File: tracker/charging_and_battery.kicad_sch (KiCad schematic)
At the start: 13 parts, among them J1 USB_C_Receptacle_PowerOnly_6P, Q1 DMG9926UDM-7, U3 DW01A, U5 TP4056-42-ESOP8

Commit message: added led's
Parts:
- added D1, D2: LED, LED_SMD:LED_0603_1608Metric, symbol Device:LED
- added R10, R8: 680, Resistor_SMD:R_0603_1608Metric, symbol Device:R
- J1: footprint Package_DFN_QFN:QFN-24-1EP_4x4mm_P0.5mm_EP2.7x2.7mm -> Connector_USB:USB_C_Receptacle_HRO_TYPE-C-31-M-12
- R4: value 2.4k -> 1.2k
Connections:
- net at C5.1, J1.A9 (VBUS), J1.B9 (VBUS)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: now also R10.1, R8.1
- net at U5.6 (~{STDBY}): now also D2.1 (K)
- net at U5.7 (~{CHRG}): now also D1.1 (K)
- new net: D2.2 (A), R10.2
- new net: D1.2 (A), R8.2
- no-connect marks 2 -> 0

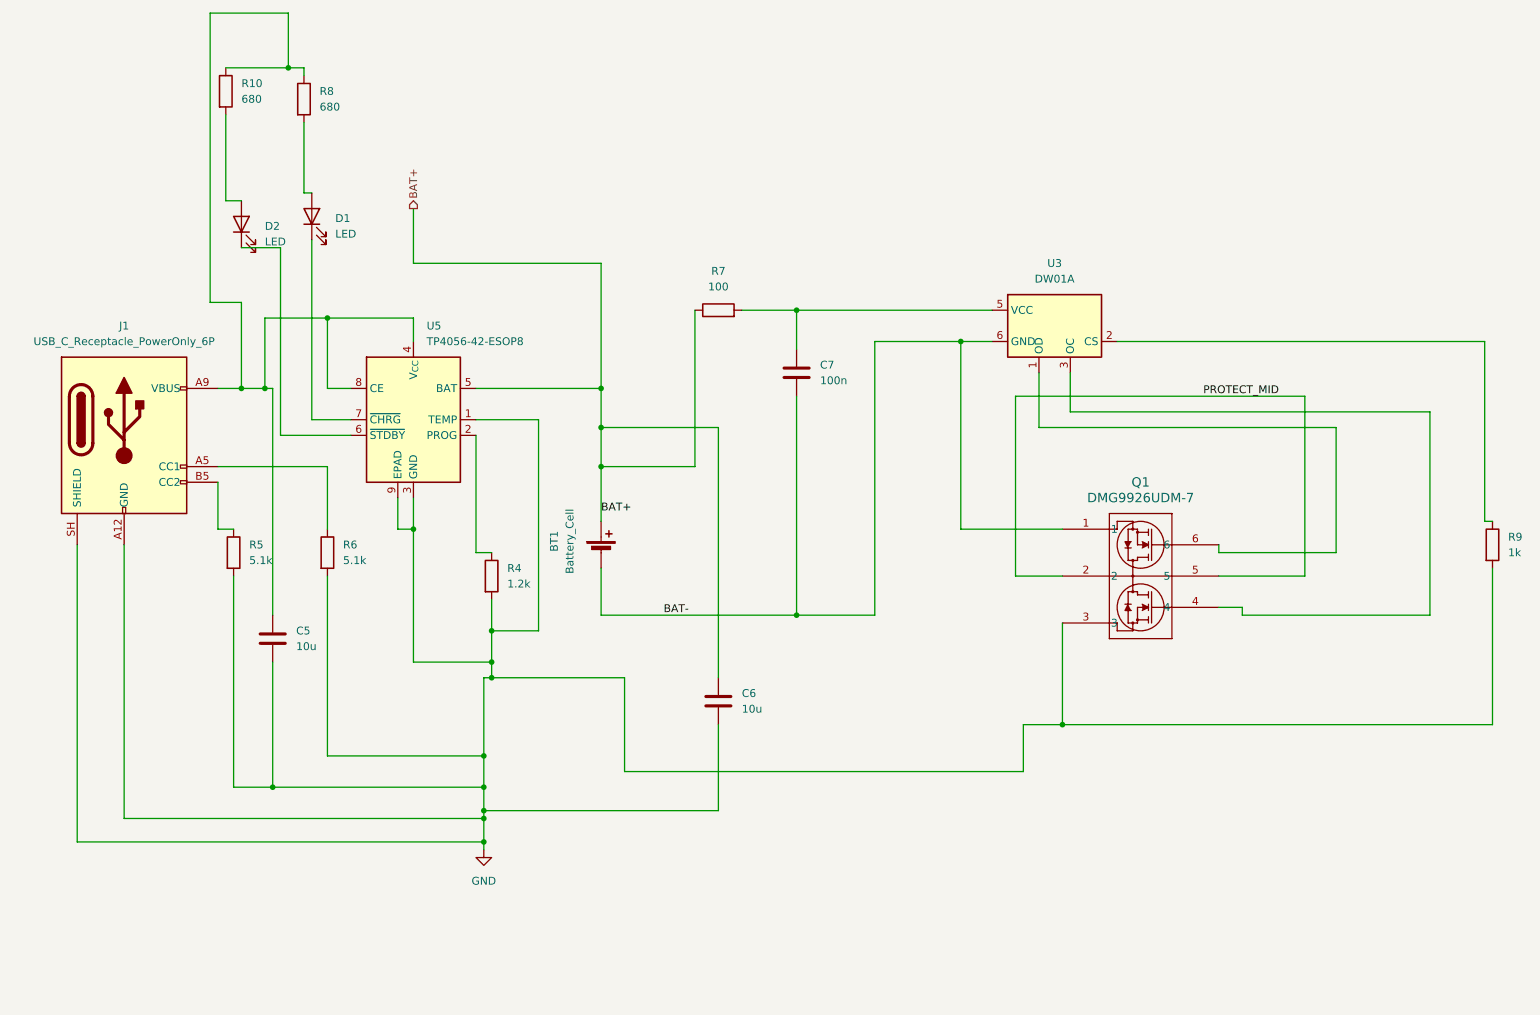
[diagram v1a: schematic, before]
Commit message: more labels on charging
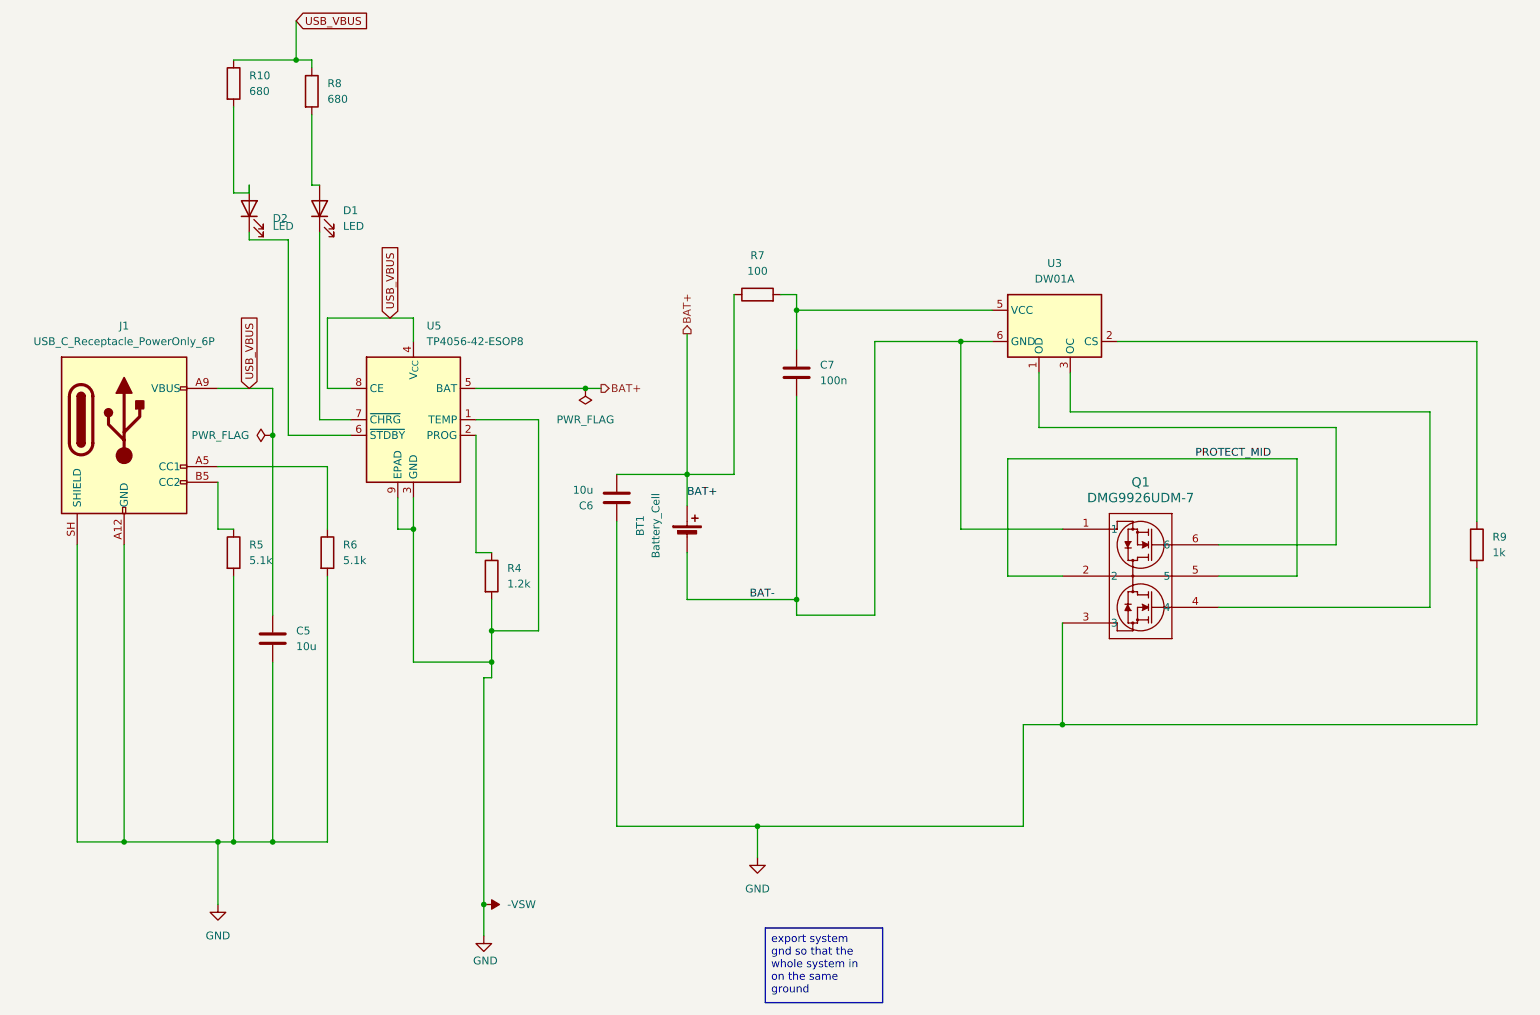
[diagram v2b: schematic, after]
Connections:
- net BAT+: now also C6.2; no longer C6.1
- net USB_VBUS: now reaches C5.1, J1.A9 (VBUS), J1.B9 (VBUS), R10.1, R8.1, U5.4 (V_{CC}), U5.8 (CE)
- net GND renamed -VSW
- net -VSW: now also C6.1; no longer C6.2
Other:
- moved on the sheet: BT1, C6, D1, D2, R10, R7, R8, R9

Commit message: started pcb design
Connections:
- net PROTECT_MID: now also R9.2
- net -VSW renamed GND
- net GND: no longer R9.2
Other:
- moved on the sheet: R9
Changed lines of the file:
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@@
-	)
-	(junction
-		(at 184.15 144.78)
-		(diameter 0)
-		(color 0 0 0 0)
 	)
 	(junction
@@
 	)
 	(junction
-		(at 90.17 173.99)
-		(diameter 0)
-		(color 0 0 0 0)
-	)
-	(junction
-		(at 134.62 161.29)
+		(at 222.25 118.11)
 		(diameter 0)
 		(color 0 0 0 0)
@@
 	)
 	(junction
-		(at 167.64 82.55)
-		(diameter 0)
-		(color 0 0 0 0)
-	)
-	(junction
 		(at 31.75 163.83)
 		(diameter 0)
@@
 	)
 	(junction
+		(at 153.67 113.03)
+		(diameter 0)
+		(color 0 0 0 0)
+	)
+	(junction
 		(at 123.19 104.14)
 		(diameter 0)
@@
 	(wire
 		(pts
-			(xy 140.97 127) (xy 153.67 127)
+			(xy 140.97 124.46) (xy 153.67 124.46)
 		)
 		(stroke
@@
 	(wire
 		(pts
+			(xy 153.67 124.46) (xy 153.67 113.03)
+		)
+		(stroke
+			(width 0)
+			(type default)
+		)
+	)
+	(wire
+		(pts
 			(xy 46.99 102.87) (xy 64.77 102.87)
 		)
@@
 	(wire
 		(pts
+			(xy 153.67 82.55) (xy 153.67 113.03)
+		)
+		(stroke
+			(width 0)
+			(type default)
+		)
+	)
+	(wire
+		(pts
 			(xy 134.62 161.29) (xy 134.62 166.37)
 		)
@@
 	(wire
 		(pts
-			(xy 251.46 111.76) (xy 251.46 82.55)
+			(xy 252.73 85.09) (xy 252.73 82.55)
 		)
 		(stroke
@@
 	(wire
 		(pts
-			(xy 222.25 101.6) (xy 222.25 120.65)
-		)
-		(stroke
-			(width 0)
-			(type default)
-		)
-	)
-	(wire
-		(pts
 			(xy 49.53 163.83) (xy 55.88 163.83)
 		)
@@
 	(wire
 		(pts
-			(xy 251.46 119.38) (xy 251.46 144.78)
+			(xy 252.73 92.71) (xy 252.73 118.11)
 		)
 		(stroke
@@
 	(wire
 		(pts
-			(xy 184.15 113.03) (xy 167.64 113.03)
-		)
-		(stroke
-			(width 0)
-			(type default)
-		)
-	)
-	(wire
-		(pts
 			(xy 58.42 66.04) (xy 52.07 66.04)
 		)
@@
 	(wire
 		(pts
-			(xy 153.67 82.55) (xy 167.64 82.55)
+			(xy 153.67 82.55) (xy 172.72 82.55)
 		)
 		(stroke
@@
 	(wire
 		(pts
-			(xy 140.97 91.44) (xy 140.97 127)
+			(xy 140.97 91.44) (xy 140.97 124.46)
 		)
 		(stroke
@@
 	(wire
 		(pts
-			(xy 177.8 144.78) (xy 177.8 161.29)
-		)
-		(stroke
-			(width 0)
-			(type default)
-		)
-	)
-	(wire
-		(pts
 			(xy 62.23 57.15) (xy 63.5 57.15)
 		)
@@
 	(wire
 		(pts
+			(xy 222.25 118.11) (xy 222.25 120.65)
+		)
+		(stroke
+			(width 0)
+			(type default)
+		)
+	)
+	(wire
+		(pts
 			(xy 243.84 125.73) (xy 243.84 93.98)
 		)
@@
 	(wire
 		(pts
-			(xy 90.17 137.16) (xy 90.17 173.99)
-		)
-		(stroke
-			(width 0)
-			(type default)
-		)
-	)
-	(wire
-		(pts
-			(xy 153.67 127) (xy 153.67 82.55)
+			(xy 172.72 144.78) (xy 184.15 144.78)
 		)
 		(stroke
@@
 	(wire
 		(pts
-			(xy 177.8 161.29) (xy 134.62 161.29)
-		)
-		(stroke
-			(width 0)
-			(type default)
-		)
-	)
-	(wire
-		(pts
 			(xy 31.75 163.83) (xy 46.99 163.83)
 		)
@@
 	(wire
 		(pts
-			(xy 184.15 144.78) (xy 251.46 144.78)
-		)
-		(stroke
-			(width 0)
-			(type default)
-		)
-	)
-	(wire
-		(pts
 			(xy 88.9 90.17) (xy 106.68 90.17)
 		)
@@
 	(wire
 		(pts
-			(xy 193.04 82.55) (xy 251.46 82.55)
+			(xy 193.04 82.55) (xy 252.73 82.55)
 		)
 		(stroke
@@
 	(wire
 		(pts
-			(xy 172.72 82.55) (xy 167.64 82.55)
-		)
-		(stroke
-			(width 0)
-			(type default)
-		)
-	)
-	(wire
-		(pts
 			(xy 180.34 96.52) (xy 180.34 87.63)
 		)
@@
 	(wire
 		(pts
-			(xy 90.17 173.99) (xy 90.17 179.07)
-		)
-		(stroke
-			(width 0)
-			(type default)
-		)
-	)
-	(wire
-		(pts
-			(xy 177.8 144.78) (xy 184.15 144.78)
+			(xy 90.17 137.16) (xy 90.17 179.07)
 		)
 		(stroke
@@
 	(wire
 		(pts
+			(xy 222.25 101.6) (xy 222.25 118.11)
+		)
+		(stroke
+			(width 0)
+			(type default)
+		)
+	)
+	(wire
+		(pts
 			(xy 209.55 115.57) (xy 228.6 115.57)
 		)
@@
 	(wire
 		(pts
-			(xy 167.64 113.03) (xy 167.64 82.55)
+			(xy 252.73 118.11) (xy 222.25 118.11)
 		)
 		(stroke
@@
 		(pts
 			(xy 24.13 163.83) (xy 31.75 163.83)
+		)
+		(stroke
+			(width 0)
+			(type default)
+		)
+	)
+	(wire
+		(pts
+			(xy 153.67 113.03) (xy 184.15 113.03)
 		)
 		(stroke
@@
 			)
 			(justify left)
+		)
+	)
+	(symbol
+		(lib_id "power:GND")
+		(at 172.72 144.78 0)
+		(unit 1)
+		(body_style 1)
+		(exclude_from_sim no)
+		(in_bom yes)
+		(on_board yes)
+		(in_pos_files yes)
+		(dnp no)
+		(fields_autoplaced yes)
+		(property "Reference" "#PWR012"
+			(at 172.72 151.13 0)
+			(hide yes)
+			(show_name no)
+			(do_not_autoplace no)
+			(effects
+				(font
+					(size 1.27 1.27)
+				)
+			)
+		)
+		(property "Value" "GND"
+			(at 172.72 149.86 0)
+			(show_name no)
+			(do_not_autoplace no)
+			(effects
+				(font
+					(size 1.27 1.27)
+				)
+			)
+		)
+		(property "Footprint" ""
+			(at 172.72 144.78 0)
+			(hide yes)
+			(show_name no)
+			(do_not_autoplace no)
+			(effects
+				(font
+					(size 1.27 1.27)
+				)
+			)
+		)
+		(property "Datasheet" ""
+			(at 172.72 144.78 0)
+			(hide yes)
+			(show_name no)
+			(do_not_autoplace no)
+			(effects
+				(font
+					(size 1.27 1.27)
+				)
+			)
+		)
+		(property "Description" "Power symbol creates a global label with name \"GND\" , ground"
+			(at 172.72 144.78 0)
+			(hide yes)
+			(show_name no)
+			(do_not_autoplace no)
+			(effects
+				(font
+					(size 1.27 1.27)
+				)
+			)
+		)
+		(pin "1"
+		)
+		(instances
+			(project "tracker"
+				(path "/0704e846-b6bf-4206-baa8-1088b529855e/c73a9412-a8df-45fb-8b45-856a5aea081b"
+					(reference "#PWR012")
+					(unit 1)
+				)
+			)
 		)
 	)
@@
 	(symbol
 		(lib_id "Device:R")
-		(at 251.46 115.57 0)
+		(at 252.73 88.9 0)
 		(unit 1)
 		(body_style 1)
@@
 		(fields_autoplaced yes)
 		(property "Reference" "R9"
-			(at 254 114.2999 0)
+			(at 255.27 87.6299 0)
 			(show_name no)
 			(do_not_autoplace no)
@@
 		)
 		(property "Value" "1k"
-			(at 254 116.8399 0)
+			(at 255.27 90.1699 0)
 			(show_name no)
 			(do_not_autoplace no)
@@
 		)
 		(property "Footprint" "Resistor_SMD:R_0603_1608Metric"
-			(at 249.682 115.57 90)
+			(at 250.952 88.9 90)
 			(hide yes)
 			(show_name no)
@@
 		)
 		(property "Datasheet" ""
-			(at 251.46 115.57 0)
+			(at 252.73 88.9 0)
 			(hide yes)
 			(show_name no)
@@
 		)
 		(property "Description" "Resistor"
-			(at 251.46 115.57 0)
+			(at 252.73 88.9 0)
 			(hide yes)
 			(show_name no)
@@
 					(unit 1)
 				)
-			)
-		)
-	)
-	(symbol
-		(lib_id "power:-VSW")
-		(at 90.17 173.99 270)
-		(unit 1)
-		(body_style 1)
-		(exclude_from_sim no)
-		(in_bom yes)
-		(on_board yes)
-		(in_pos_files yes)
-		(dnp no)
-		(fields_autoplaced yes)
-		(property "Reference" "#PWR010"
-			(at 86.36 173.99 0)
-			(hide yes)
-			(show_name no)
-			(do_not_autoplace no)
-			(effects
-				(font
-					(size 1.27 1.27)
-				)
-			)
-		)
-		(property "Value" "-VSW"
-			(at 93.98 173.9899 90)
-			(show_name no)
-			(do_not_autoplace no)
-			(effects
-				(font
-					(size 1.27 1.27)
-				)
-				(justify left)
-			)
-		)
-		(property "Footprint" ""
-			(at 90.17 173.99 0)
-			(hide yes)
-			(show_name no)
-			(do_not_autoplace no)
-			(effects
-				(font
-					(size 1.27 1.27)
-				)
-			)
-		)
-		(property "Datasheet" ""
-			(at 90.17 173.99 0)
-			(hide yes)
-			(show_name no)
-			(do_not_autoplace no)
-			(effects
-				(font
-					(size 1.27 1.27)
-				)
-			)
-		)
-		(property "Description" "Power symbol creates a global label with name \"-VSW\""
-			(at 90.17 173.99 0)
-			(hide yes)
-			(show_name no)
-			(do_not_autoplace no)
-			(effects
-				(font
-					(size 1.27 1.27)
-				)
-			)
-		)
-		(pin "1"
-		)
-		(instances
-			(project "tracker"
-				(path "/0704e846-b6bf-4206-baa8-1088b529855e/c73a9412-a8df-45fb-8b45-856a5aea081b"
-					(reference "#PWR010")
-					(unit 1)
-				)

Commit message: working on ground
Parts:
- J1: footprint Connector_USB:USB_C_Receptacle_HRO_TYPE-C-31-M-12 -> Connector_USB:USB_C_Receptacle_GCT_USB4125-xx-x-0190_6P_TopMnt_Horizontal
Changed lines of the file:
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@@
 			)
 		)
-		(property "Footprint" "Connector_USB:USB_C_Receptacle_HRO_TYPE-C-31-M-12"
+		(property "Footprint" "Connector_USB:USB_C_Receptacle_GCT_USB4125-xx-x-0190_6P_TopMnt_Horizontal"
 			(at 35.56 95.25 0)
 			(hide yes)

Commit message: made pcb . bpm , cpl
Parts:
- Q1: footprint SOT-26_DIO -> dikigey_dual_channel_nfets:SOT-26_DIO
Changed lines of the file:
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@@
 			)
 		)
-		(property "Footprint" "SOT-26_DIO"
+		(property "Footprint" "dikigey_dual_channel_nfets:SOT-26_DIO"
 			(at 184.15 113.03 0)
 			(hide yes)
